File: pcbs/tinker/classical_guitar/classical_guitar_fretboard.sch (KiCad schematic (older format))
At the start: 172 parts, among them U1 AT42QT1110-A, U2 AT42QT1110-A, U3 AT42QT1110-A

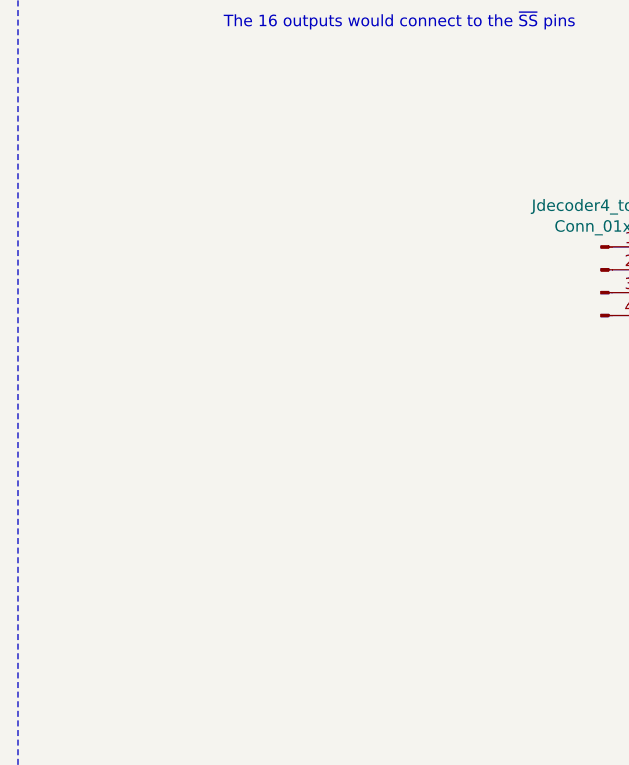
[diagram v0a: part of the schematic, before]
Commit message: Replaced CD74HC154ME4 with faster CD74GC4515M with latch
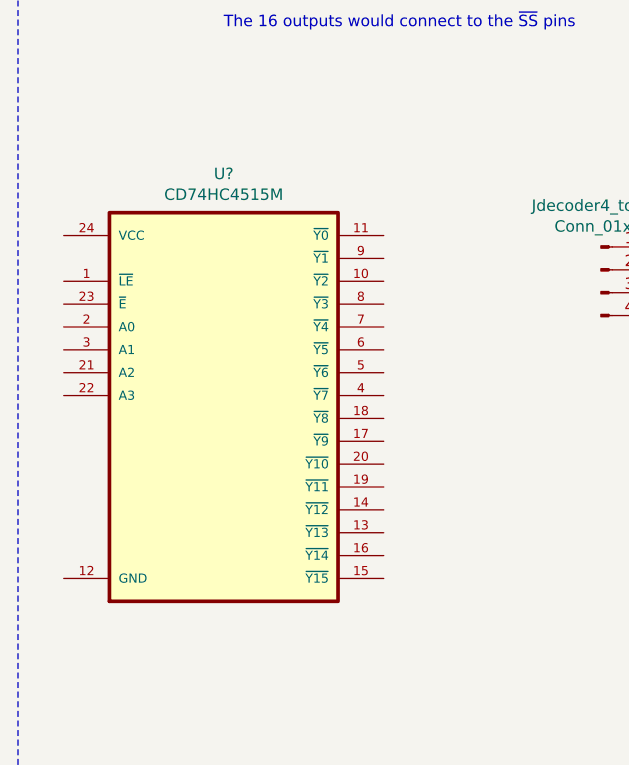
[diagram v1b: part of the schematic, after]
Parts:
- added U?: CD74HC4515M, SOIC127P1030X265-24N, symbol Custom_74xx:CD74HC4515M
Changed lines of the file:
@@
+	1    0    0    -1
+$EndComp
+$Comp
+L Custom_74xx:CD74HC4515M U?
+U 1 1 61A715CC
+P 1400 6250
+F 0 "U?" H 1400 7420 50  0000 C CNN
+F 1 "CD74HC4515M" H 1400 7329 50  0000 C CNN
+F 2 "SOIC127P1030X265-24N" H 1000 7300 50  0001 L BNN
+F 3 "" H 1400 6250 50  0001 L BNN
+	1    1400 6250
 	1    0    0    -1
 $EndComp

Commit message: Prepare electrode tracking
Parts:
- removed Jdecoder4_to_16_input1: Conn_01x04_Male, Connector_PinSocket_2.54mm:PinSocket_1x04_P2.54mm_Vertical, symbol Connector:Conn_01x04_Male
- removed Udecoder4_to_161: CD74HC154ME4, Package_SO:SOIC-24W_7.5x15.4mm_P1.27mm, symbol Custom_74xx:CD74HC154ME4
- added Jdecoder4_to_16_input1: Conn_01x06_Male, Connector_PinHeader_2.54mm:PinHeader_1x06_P2.54mm_Vertical, symbol Connector:Conn_01x06_Male
- Dec1: renamed from U?; footprint SOIC127P1030X265-24N -> Package_SO:SOIC-24W_7.5x15.4mm_P1.27mm
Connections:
- net GND: now also Dec1.12 (GND)
- net VDD: now also Dec1.24 (VCC)
- net at Dec1.1 (~LE): now also Jdecoder4_to_16_input1.1 (Pin_1)
- net at Dec1.10 (~Y2): now also Jdecoder4_to_16_output1.3 (Pin_3)
- net at Dec1.11 (~Y0): now also Jdecoder4_to_16_output1.1 (Pin_1)
- net at Dec1.13 (~Y13): now also Jdecoder4_to_16_output1.14 (Pin_14)
- net at Dec1.14 (~Y12): now also Jdecoder4_to_16_output1.13 (Pin_13)
- net at Dec1.15 (~Y15): now also Jdecoder4_to_16_output1.16 (Pin_16)
- net at Dec1.16 (~Y14): now also Jdecoder4_to_16_output1.15 (Pin_15)
- net at Dec1.17 (~Y9): now also Jdecoder4_to_16_output1.10 (Pin_10)
- net at Dec1.18 (~Y8): now also Jdecoder4_to_16_output1.9 (Pin_9)
- net at Dec1.19 (~Y11): now also Jdecoder4_to_16_output1.12 (Pin_12)
- net at Dec1.2 (A0): now also Jdecoder4_to_16_input1.3 (Pin_3)
- net at Dec1.20 (~Y10): now also Jdecoder4_to_16_output1.11 (Pin_11)
- net at Dec1.21 (A2): now also Jdecoder4_to_16_input1.5 (Pin_5)
- net at Dec1.22 (A3): now also Jdecoder4_to_16_input1.6 (Pin_6)
- net at Dec1.23 (~E): now also Jdecoder4_to_16_input1.2 (Pin_2)
- net at Dec1.3 (A1): now also Jdecoder4_to_16_input1.4 (Pin_4)
- net at Dec1.4 (~Y7): now also Jdecoder4_to_16_output1.8 (Pin_8)
- net at Dec1.5 (~Y6): now also Jdecoder4_to_16_output1.7 (Pin_7)
- net at Dec1.6 (~Y5): now also Jdecoder4_to_16_output1.6 (Pin_6)
- net at Dec1.7 (~Y4): now also Jdecoder4_to_16_output1.5 (Pin_5)
- net at Dec1.8 (~Y3): now also Jdecoder4_to_16_output1.4 (Pin_4)
- net at Dec1.9 (~Y1): now also Jdecoder4_to_16_output1.2 (Pin_2)
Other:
- moved on the sheet: Dec1, Jpower1
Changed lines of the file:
@@
 L Connector:Conn_01x04_Male Jpower1
 U 1 1 62667B26
-P 7300 3200
-F 0 "Jpower1" H 7408 3481 50  0000 C CNN
-F 1 "Conn_01x04_Male" H 7408 3390 50  0000 C CNN
-F 2 "Connector_PinSocket_2.54mm:PinSocket_1x04_P2.54mm_Vertical" H 7300 3200 50  0001 C CNN
-F 3 "~" H 7300 3200 50  0001 C CNN
-	1    7300 3200
+P 6750 3050
+F 0 "Jpower1" H 6858 3331 50  0000 C CNN
+F 1 "Conn_01x04_Male" H 6858 3240 50  0000 C CNN
+F 2 "Connector_PinSocket_2.54mm:PinSocket_1x04_P2.54mm_Vertical" H 6750 3050 50  0001 C CNN
+F 3 "~" H 6750 3050 50  0001 C CNN
+	1    6750 3050
 	1    0    0    -1
 $EndComp
@@
 L power:VDD #PWR02
 U 1 1 6266B77C
-P 7600 3000
-F 0 "#PWR02" H 7600 2850 50  0001 C CNN
-F 1 "VDD" H 7615 3173 50  0000 C CNN
-F 2 "" H 7600 3000 50  0001 C CNN
-F 3 "" H 7600 3000 50  0001 C CNN
-	1    7600 3000
+P 7050 2850
+F 0 "#PWR02" H 7050 2700 50  0001 C CNN
+F 1 "VDD" H 7065 3023 50  0000 C CNN
+F 2 "" H 7050 2850 50  0001 C CNN
+F 3 "" H 7050 2850 50  0001 C CNN
+	1    7050 2850
 	1    0    0    -1
 $EndComp
@@
 L power:GND #PWR03
 U 1 1 6266C1F3
-P 7600 3500
-F 0 "#PWR03" H 7600 3250 50  0001 C CNN
-F 1 "GND" H 7605 3327 50  0000 C CNN
-F 2 "" H 7600 3500 50  0001 C CNN
-F 3 "" H 7600 3500 50  0001 C CNN
-	1    7600 3500
-	1    0    0    -1
-$EndComp
-Wire Wire Line
-	7500 3100 7600 3100
-Wire Wire Line
-	7600 3100 7600 3000
-Wire Wire Line
-	7500 3200 7600 3200
-Wire Wire Line
-	7600 3200 7600 3100
-Connection ~ 7600 3100
-Wire Wire Line
-	7500 3300 7600 3300
-Wire Wire Line
-	7600 3300 7600 3400
-Wire Wire Line
-	7500 3400 7600 3400
-Connection ~ 7600 3400
-Wire Wire Line
-	7600 3400 7600 3500
+P 7050 3350
+F 0 "#PWR03" H 7050 3100 50  0001 C CNN
+F 1 "GND" H 7055 3177 50  0000 C CNN
+F 2 "" H 7050 3350 50  0001 C CNN
+F 3 "" H 7050 3350 50  0001 C CNN
+	1    7050 3350
+	1    0    0    -1
+$EndComp
+Wire Wire Line
+	6950 2950 7050 2950
+Wire Wire Line
+	7050 2950 7050 2850
+Wire Wire Line
+	6950 3050 7050 3050
+Wire Wire Line
+	7050 3050 7050 2950
+Connection ~ 7050 2950
+Wire Wire Line
+	6950 3150 7050 3150
+Wire Wire Line
+	7050 3150 7050 3250
+Wire Wire Line
+	6950 3250 7050 3250
+Connection ~ 7050 3250
+Wire Wire Line
+	7050 3250 7050 3350
 Wire Notes Line
 	500  500  8450 500
@@
 Text Label 2650 10650 2    50   ~ 0
 MOSI1
-Wire Notes Line
-	8450 500  8450 25650
 $Comp
 L Custom_Sensor_Touch:Electrode E30
@@
 $EndComp
 $Comp
-L Custom_74xx:CD74HC154ME4 Udecoder4_to_161
-U 1 1 6445F660
+L Connector_Generic:Conn_01x16 Jdecoder4_to_16_output1
+U 1 1 61AB5D90
+P 4850 6000
+F 0 "Jdecoder4_to_16_output1" H 4930 5992 50  0000 L CNN
+F 1 "Conn_01x16" H 4930 5901 50  0000 L CNN
+F 2 "Connector_PinSocket_2.54mm:PinSocket_1x16_P2.54mm_Vertical" H 4850 6000 50  0001 C CNN
+F 3 "~" H 4850 6000 50  0001 C CNN
+	1    4850 6000
+	1    0    0    -1
+$EndComp
+$Comp
+L power:GND #PWR0101
+U 1 1 61AB76EE
+P 3250 6800
+F 0 "#PWR0101" H 3250 6550 50  0001 C CNN
+F 1 "GND" H 3255 6627 50  0000 C CNN
+F 2 "" H 3250 6800 50  0001 C CNN
+F 3 "" H 3250 6800 50  0001 C CNN
+	1    3250 6800
+	1    0    0    -1
+$EndComp
+$Comp
+L power:VDD #PWR0102
+U 1 1 61AB8023
+P 3250 5300
+F 0 "#PWR0102" H 3250 5150 50  0001 C CNN
+F 1 "VDD" H 3265 5473 50  0000 C CNN
+F 2 "" H 3250 5300 50  0001 C CNN
+F 3 "" H 3250 5300 50  0001 C CNN
+	1    3250 5300
+	1    0    0    -1
+$EndComp
+Wire Notes Line
+	8450 500  8450 25650
+$Comp
+L Connector:Conn_01x06_Male Jdecoder4_to_16_input1
+U 1 1 61C900AB
+P 3050 5700
+F 0 "Jdecoder4_to_16_input1" H 3158 6081 50  0000 C CNN
+F 1 "Conn_01x06_Male" H 3158 5990 50  0000 C CNN
+F 2 "Connector_PinHeader_2.54mm:PinHeader_1x06_P2.54mm_Vertical" H 3050 5700 50  0001 C CNN
+F 3 "~" H 3050 5700 50  0001 C CNN
+	1    3050 5700
+	1    0    0    -1
+$EndComp
+$Comp
+L Custom_74xx:CD74HC4515M Dec1
+U 1 1 61A715CC
 P 3950 6200
-F 0 "Udecoder4_to_161" H 3950 7470 50  0000 C CNN
-F 1 "CD74HC154ME4" H 3950 7379 50  0000 C CNN
-F 2 "Package_SO:SOIC-24W_7.5x15.4mm_P1.27mm" H 3550 7350 50  0001 L BNN
+F 0 "Dec1" H 3950 7370 50  0000 C CNN
+F 1 "CD74HC4515M" H 3950 7279 50  0000 C CNN
+F 2 "Package_SO:SOIC-24W_7.5x15.4mm_P1.27mm" H 3550 7250 50  0001 L BNN
 F 3 "" H 3950 6200 50  0001 L BNN
 	1    3950 6200
 	1    0    0    -1
 $EndComp
-$Comp
-L power:GND #PWR021
-U 1 1 644A4F53
-P 3250 6000
-F 0 "#PWR021" H 3250 5750 50  0001 C CNN
-F 1 "GND" H 3255 5827 50  0000 C CNN
-F 2 "" H 3250 6000 50  0001 C CNN
-F 3 "" H 3250 6000 50  0001 C CNN
-	1    3250 6000
-	1    0    0    -1
-$EndComp
-Wire Wire Line
-	3250 5800 3250 5900
-Connection ~ 3250 5900
-Wire Wire Line
-	3250 5900 3250 6000
-$Comp
-L power:GND #PWR023
-U 1 1 644EA8EE
-P 4650 7300
-F 0 "#PWR023" H 4650 7050 50  0001 C CNN
-F 1 "GND" H 4655 7127 50  0000 C CNN
-F 2 "" H 4650 7300 50  0001 C CNN
-F 3 "" H 4650 7300 50  0001 C CNN
-	1    4650 7300
-	1    0    0    -1
-$EndComp
-Wire Wire Line
-	4650 7200 4650 7300
-$Comp
-L power:VDD #PWR022
-U 1 1 6450E3BE
-P 4650 5100
-F 0 "#PWR022" H 4650 4950 50  0001 C CNN
-F 1 "VDD" H 4665 5273 50  0000 C CNN
-F 2 "" H 4650 5100 50  0001 C CNN
-F 3 "" H 4650 5100 50  0001 C CNN
-	1    4650 5100
-	1    0    0    -1
-$EndComp
-Wire Wire Line
-	4650 5100 4650 5200
-$Comp
-L Connector_Generic:Conn_01x16 Jdecoder4_to_16_output1
-U 1 1 6453313E
-P 4850 6100
-F 0 "Jdecoder4_to_16_output1" H 4930 6092 50  0000 L CNN
-F 1 "Conn_01x16" H 4930 6001 50  0000 L CNN
-F 2 "Connector_PinSocket_2.54mm:PinSocket_1x16_P2.54mm_Vertical" H 4850 6100 50  0001 C CNN
-F 3 "~" H 4850 6100 50  0001 C CNN
-	1    4850 6100
-	1    0    0    -1
-$EndComp
-$Comp
-L Connector:Conn_01x04_Male Jdecoder4_to_16_input1
-U 1 1 6455E6EE
-P 3050 5500
-F 0 "Jdecoder4_to_16_input1" H 3158 5781 50  0000 C CNN
-F 1 "Conn_01x04_Male" H 3158 5690 50  0000 C CNN
-F 2 "Connector_PinSocket_2.54mm:PinSocket_1x04_P2.54mm_Vertical" H 3050 5500 50  0001 C CNN
-F 3 "~" H 3050 5500 50  0001 C CNN
-	1    3050 5500
-	1    0    0    -1
-$EndComp
-$Comp
-L Custom_74xx:CD74HC4515M U?
-U 1 1 61A715CC
-P 1400 6250
-F 0 "U?" H 1400 7420 50  0000 C CNN
-F 1 "CD74HC4515M" H 1400 7329 50  0000 C CNN
-F 2 "SOIC127P1030X265-24N" H 1000 7300 50  0001 L BNN
-F 3 "" H 1400 6250 50  0001 L BNN
-	1    1400 6250
-	1    0    0    -1
-$EndComp
